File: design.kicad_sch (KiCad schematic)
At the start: 92 parts, among them J1 2601-3108, J10 Conn_01x04, J11 Conn_01x04, J12 Conn_01x03, J13 Conn_01x03, J14 BM04B-SRSS-TB_LF__SN_, J2 2601-3108, J3 2601-3108, J4 TYPE-C-31-M-12, J5 SKEDD-UPDI-4, J6 Conn_01x04, J7 Conn_01x04, J8 Conn_01x04, J9 Conn_01x04, Q1 AO3400A, Q2 AO3400A, SW1 K3-2235S-K1, SW2 K3-2235S-K1, U1 ATtiny1616-S, U2 AP2112K-3.3, U3 CP2105, U4 ATtiny1616-M

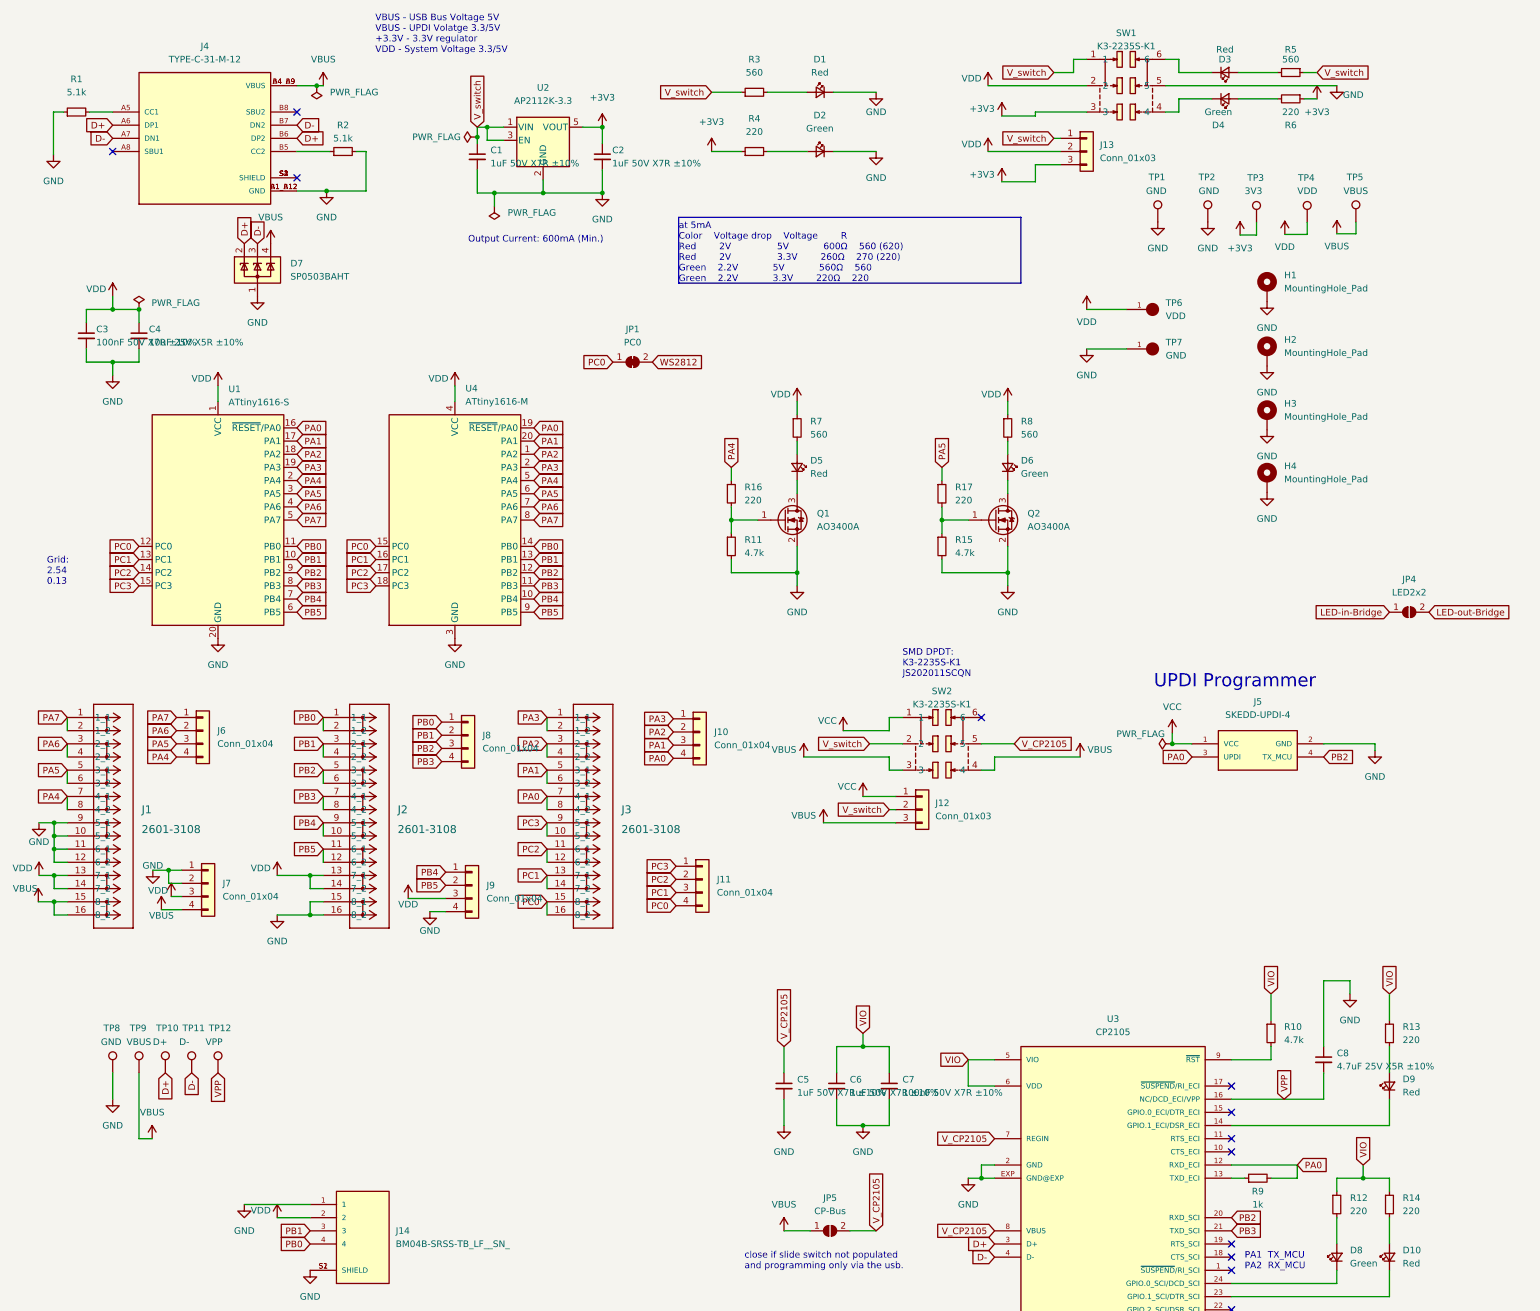
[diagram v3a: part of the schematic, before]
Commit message: add resistor variance
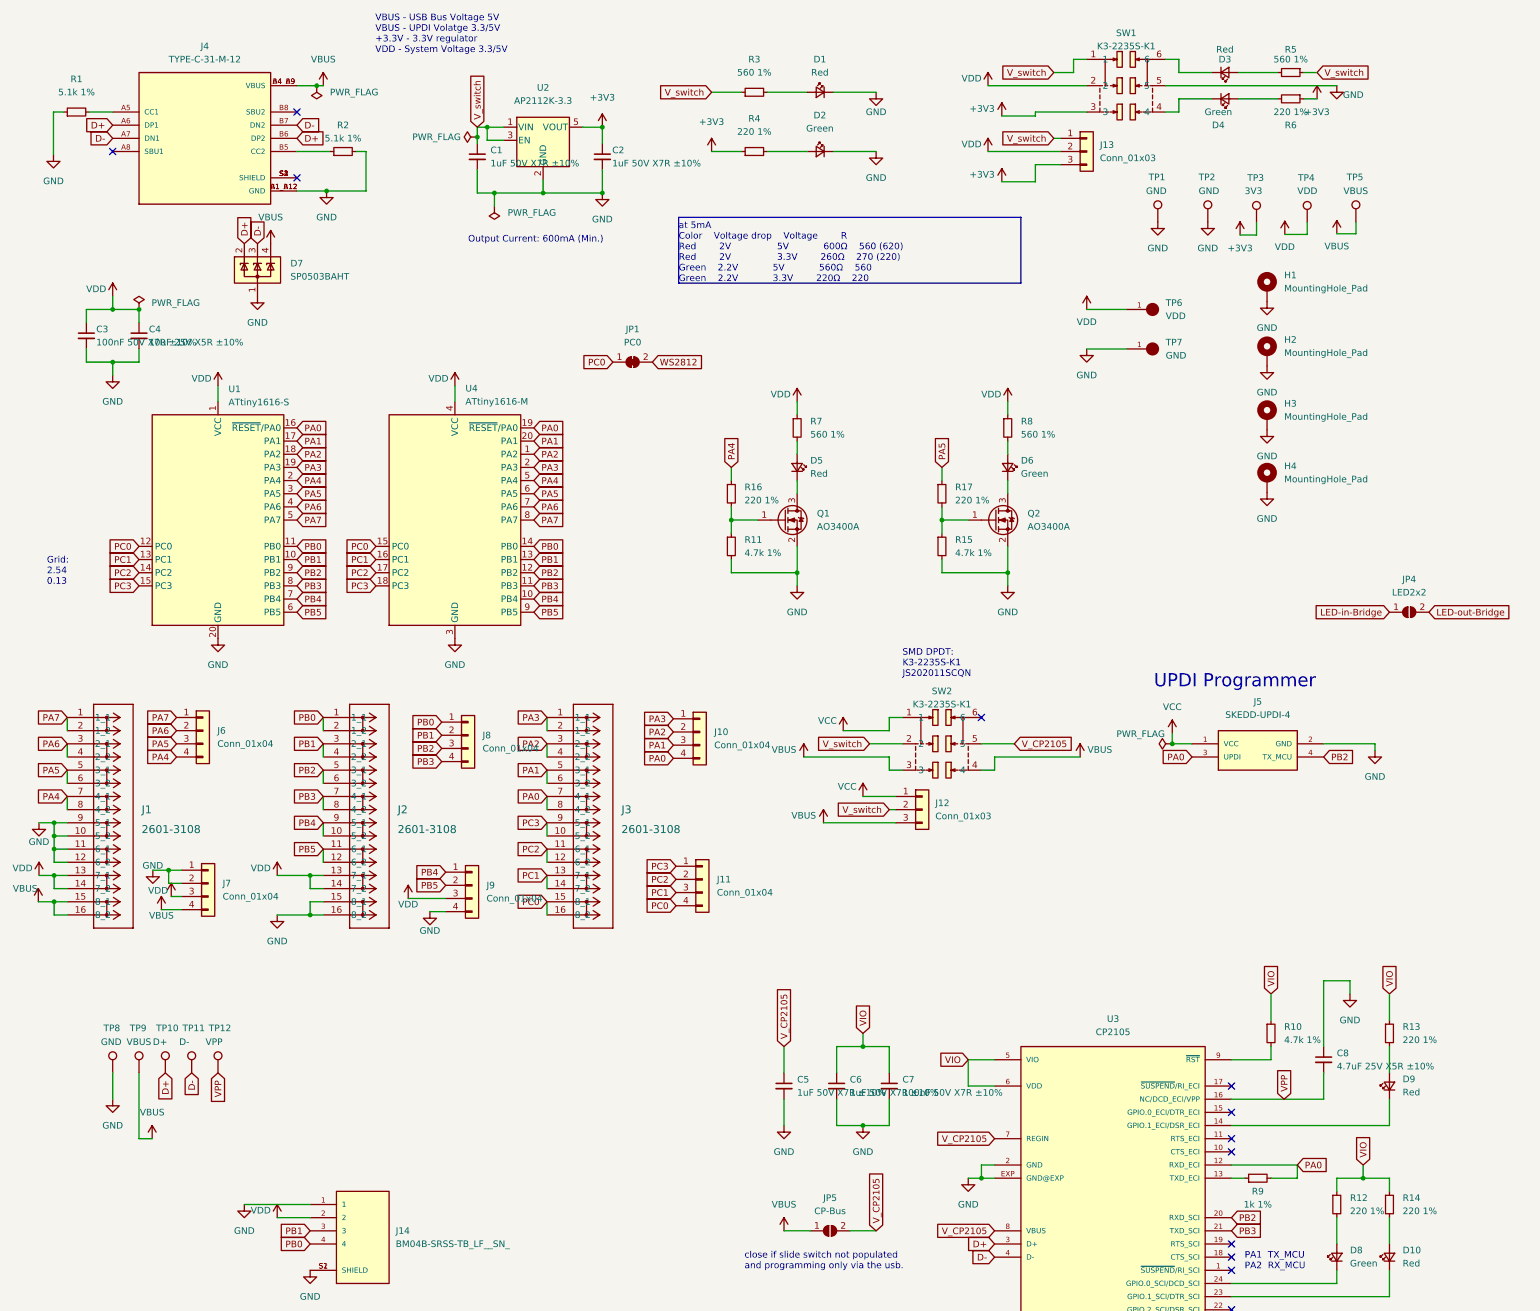
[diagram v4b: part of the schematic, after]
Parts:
- R1, R2: value 5.1k -> 5.1k 1%
- R10, R11, R15: value 4.7k -> 4.7k 1%
- R12, R13, R14, R16, R17, R4, R6: value 220 -> 220 1%
- R3, R5, R7, R8: value 560 -> 560 1%
- R9: value 1k -> 1k 1%
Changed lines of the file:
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@@
       (effects (font (size 1.27 1.27)) (justify left))
     )
-    (property "Value" "220" (id 1) (at 154.94 107.9499 0)
+    (property "Value" "220 1%" (id 1) (at 154.94 107.9499 0)
       (effects (font (size 1.27 1.27)) (justify left))
     )
@@
     (in_bom yes) (on_board yes) (fields_autoplaced)
     (property "Reference" "R4" (id 0) (at 156.845 34.29 90))
-    (property "Value" "220" (id 1) (at 156.845 36.83 90))
+    (property "Value" "220 1%" (id 1) (at 156.845 36.83 90))
     (property "Footprint" "Resistor_SMD:R_0805_2012Metric" (id 2) (at 156.845 40.64 0)
       (effects (font (size 1.27 1.27)) hide)
@@
       (effects (font (size 1.27 1.27)) (justify left))
     )
-    (property "Value" "220" (id 1) (at 195.58 107.9499 0)
+    (property "Value" "220 1%" (id 1) (at 195.58 107.9499 0)
       (effects (font (size 1.27 1.27)) (justify left))
     )
@@
     (in_bom yes) (on_board yes)
     (property "Reference" "R1" (id 0) (at 26.035 26.67 90))
-    (property "Value" "5.1k" (id 1) (at 26.035 29.21 90))
+    (property "Value" "5.1k 1%" (id 1) (at 26.035 29.21 90))
     (property "Footprint" "Resistor_SMD:R_0805_2012Metric" (id 2) (at 26.035 33.02 0)
       (effects (font (size 1.27 1.27)) hide)
@@
       (effects (font (size 1.27 1.27)) (justify left))
     )
-    (property "Value" "560" (id 1) (at 167.64 95.2499 0)
+    (property "Value" "560 1%" (id 1) (at 167.64 95.2499 0)
       (effects (font (size 1.27 1.27)) (justify left))
     )
@@
       (effects (font (size 1.27 1.27)) (justify left))
     )
-    (property "Value" "560" (id 1) (at 208.28 95.2499 0)
+    (property "Value" "560 1%" (id 1) (at 208.28 95.2499 0)
       (effects (font (size 1.27 1.27)) (justify left))
     )
@@
     (in_bom yes) (on_board yes) (fields_autoplaced)
     (property "Reference" "R3" (id 0) (at 156.845 22.86 90))
-    (property "Value" "560" (id 1) (at 156.845 25.4 90))
+    (property "Value" "560 1%" (id 1) (at 156.845 25.4 90))
     (property "Footprint" "Resistor_SMD:R_0805_2012Metric" (id 2) (at 156.845 29.21 0)
       (effects (font (size 1.27 1.27)) hide)
@@
       (effects (font (size 1.27 1.27)) (justify left))
     )
-    (property "Value" "220" (id 1) (at 281.94 245.1099 0)
+    (property "Value" "220 1%" (id 1) (at 281.94 245.1099 0)
       (effects (font (size 1.27 1.27)) (justify left))
     )
@@
     (in_bom yes) (on_board yes)
     (property "Reference" "R9" (id 0) (at 254 241.3 90))
-    (property "Value" "1k" (id 1) (at 254 243.84 90))
+    (property "Value" "1k 1%" (id 1) (at 254 243.84 90))
     (property "Footprint" "Resistor_SMD:R_0805_2012Metric" (id 2) (at 254 238.76 0)
       (effects (font (size 1.27 1.27)) hide)
@@
     (in_bom yes) (on_board yes)
     (property "Reference" "R6" (id 0) (at 260.35 35.56 90))
-    (property "Value" "220" (id 1) (at 260.35 33.02 90))
+    (property "Value" "220 1%" (id 1) (at 260.35 33.02 90))
     (property "Footprint" "Resistor_SMD:R_0805_2012Metric" (id 2) (at 260.35 30.48 0)
       (effects (font (size 1.27 1.27)) hide)
@@
       (effects (font (size 1.27 1.27)) (justify left))
     )
-    (property "Value" "4.7k" (id 1) (at 259.08 212.0899 0)
+    (property "Value" "4.7k 1%" (id 1) (at 259.08 212.0899 0)
       (effects (font (size 1.27 1.27)) (justify left))
     )
@@
       (effects (font (size 1.27 1.27)) (justify left))
     )
-    (property "Value" "220" (id 1) (at 281.94 212.0899 0)
+    (property "Value" "220 1%" (id 1) (at 281.94 212.0899 0)
       (effects (font (size 1.27 1.27)) (justify left))
     )
@@
     (in_bom yes) (on_board yes)
     (property "Reference" "R5" (id 0) (at 260.35 20.955 90))
-    (property "Value" "560" (id 1) (at 260.35 22.86 90))
+    (property "Value" "560 1%" (id 1) (at 260.35 22.86 90))
     (property "Footprint" "Resistor_SMD:R_0805_2012Metric" (id 2) (at 260.35 25.4 0)
       (effects (font (size 1.27 1.27)) hide)
@@
     (in_bom yes) (on_board yes)
     (property "Reference" "R2" (id 0) (at 77.47 35.56 90))
-    (property "Value" "5.1k" (id 1) (at 77.47 38.1 90))
+    (property "Value" "5.1k 1%" (id 1) (at 77.47 38.1 90))
     (property "Footprint" "Resistor_SMD:R_0805_2012Metric" (id 2) (at 77.47 40.64 0)
       (effects (font (size 1.27 1.27)) hide)
@@
       (effects (font (size 1.27 1.27)) (justify left))
     )
-    (property "Value" "220" (id 1) (at 271.78 245.1099 0)
+    (property "Value" "220 1%" (id 1) (at 271.78 245.1099 0)
       (effects (font (size 1.27 1.27)) (justify left))
     )
@@
       (effects (font (size 1.27 1.27)) (justify left))
     )
-    (property "Value" "4.7k" (id 1) (at 154.94 118.1099 0)
+    (property "Value" "4.7k 1%" (id 1) (at 154.94 118.1099 0)
       (effects (font (size 1.27 1.27)) (justify left))
     )
@@
       (effects (font (size 1.27 1.27)) (justify left))
     )
-    (property "Value" "4.7k" (id 1) (at 195.58 118.1099 0)
+    (property "Value" "4.7k 1%" (id 1) (at 195.58 118.1099 0)
       (effects (font (size 1.27 1.27)) (justify left))
     )
@@
     )
     (path "/2d960c53-92c0-4508-8c86-63a3901a9176"
-      (reference "R1") (unit 1) (value "5.1k") (footprint "Resistor_SMD:R_0805_2012Metric")
+      (reference "R1") (unit 1) (value "5.1k 1%") (footprint "Resistor_SMD:R_0805_2012Metric")
     )
     (path "/c779e7c4-17e4-477d-a6d1-52b907c8df98"
-      (reference "R2") (unit 1) (value "5.1k") (footprint "Resistor_SMD:R_0805_2012Metric")
+      (reference "R2") (unit 1) (value "5.1k 1%") (footprint "Resistor_SMD:R_0805_2012Metric")
     )
     (path "/484da902-60c6-4980-9a91-4f667955b0e8"
-      (reference "R3") (unit 1) (value "560") (footprint "Resistor_SMD:R_0805_2012Metric")
+      (reference "R3") (unit 1) (value "560 1%") (footprint "Resistor_SMD:R_0805_2012Metric")
     )
     (path "/0e89c407-3205-4c62-a491-3291420c5ad0"
-      (reference "R4") (unit 1) (value "220") (footprint "Resistor_SMD:R_0805_2012Metric")
+      (reference "R4") (unit 1) (value "220 1%") (footprint "Resistor_SMD:R_0805_2012Metric")
     )
     (path "/bcf61e20-6cf8-46b9-9f95-d5e631d20676"
-      (reference "R5") (unit 1) (value "560") (footprint "Resistor_SMD:R_0805_2012Metric")
+      (reference "R5") (unit 1) (value "560 1%") (footprint "Resistor_SMD:R_0805_2012Metric")
     )
     (path "/72f13b47-0aa0-4ea7-a1ab-fd196a1c1813"
-      (reference "R6") (unit 1) (value "220") (footprint "Resistor_SMD:R_0805_2012Metric")
+      (reference "R6") (unit 1) (value "220 1%") (footprint "Resistor_SMD:R_0805_2012Metric")
     )
     (path "/42965c34-d4b3-417b-ac70-1b8024990edc"
-      (reference "R7") (unit 1) (value "560") (footprint "Resistor_SMD:R_0805_2012Metric")
+      (reference "R7") (unit 1) (value "560 1%") (footprint "Resistor_SMD:R_0805_2012Metric")
     )
     (path "/44e2dfc4-2c8c-4871-9b80-83ccfe223af7"
-      (reference "R8") (unit 1) (value "560") (footprint "Resistor_SMD:R_0805_2012Metric")
+      (reference "R8") (unit 1) (value "560 1%") (footprint "Resistor_SMD:R_0805_2012Metric")
     )
     (path "/5d57726e-0434-4089-b57f-b38108417a5f"
-      (reference "R9") (unit 1) (value "1k") (footprint "Resistor_SMD:R_0805_2012Metric")
+      (reference "R9") (unit 1) (value "1k 1%") (footprint "Resistor_SMD:R_0805_2012Metric")
     )
     (path "/97ff0e12-c8c6-4e4c-ac54-7a23a9d49f5e"
-      (reference "R10") (unit 1) (value "4.7k") (footprint "Resistor_SMD:R_0805_2012Metric")
+      (reference "R10") (unit 1) (value "4.7k 1%") (footprint "Resistor_SMD:R_0805_2012Metric")
     )
     (path "/eae5ea89-345f-400b-bbc1-315b0f92403d"
-      (reference "R11") (unit 1) (value "4.7k") (footprint "Resistor_SMD:R_0805_2012Metric")
+      (reference "R11") (unit 1) (value "4.7k 1%") (footprint "Resistor_SMD:R_0805_2012Metric")
     )
     (path "/d3f3b6a4-65f9-4d68-88bb-38ec87453a14"
-      (reference "R12") (unit 1) (value "220") (footprint "Resistor_SMD:R_0805_2012Metric")
+      (reference "R12") (unit 1) (value "220 1%") (footprint "Resistor_SMD:R_0805_2012Metric")
     )
     (path "/a758422c-1795-447b-8ef1-8283da654354"
-      (reference "R13") (unit 1) (value "220") (footprint "Resistor_SMD:R_0805_2012Metric")
+      (reference "R13") (unit 1) (value "220 1%") (footprint "Resistor_SMD:R_0805_2012Metric")
     )
     (path "/5799ac00-06e7-4fa3-91a4-ef96b7ec0384"
-      (reference "R14") (unit 1) (value "220") (footprint "Resistor_SMD:R_0805_2012Metric")
+      (reference "R14") (unit 1) (value "220 1%") (footprint "Resistor_SMD:R_0805_2012Metric")
     )
     (path "/fa4d6553-7f09-4a6e-9c40-3ec022302ac5"
-      (reference "R15") (unit 1) (value "4.7k") (footprint "Resistor_SMD:R_0805_2012Metric")
+      (reference "R15") (unit 1) (value "4.7k 1%") (footprint "Resistor_SMD:R_0805_2012Metric")
     )
     (path "/054880c8-c6d2-48c6-bac5-eb0eb8670720"
-      (reference "R16") (unit 1) (value "220") (footprint "Resistor_SMD:R_0805_2012Metric")
+      (reference "R16") (unit 1) (value "220 1%") (footprint "Resistor_SMD:R_0805_2012Metric")
     )
     (path "/184973bb-9061-457b-885d-f342e181cc30"
-      (reference "R17") (unit 1) (value "220") (footprint "Resistor_SMD:R_0805_2012Metric")
+      (reference "R17") (unit 1) (value "220 1%") (footprint "Resistor_SMD:R_0805_2012Metric")
     )
     (path "/3c015059-970d-4b9b-a360-1a6bff162160"

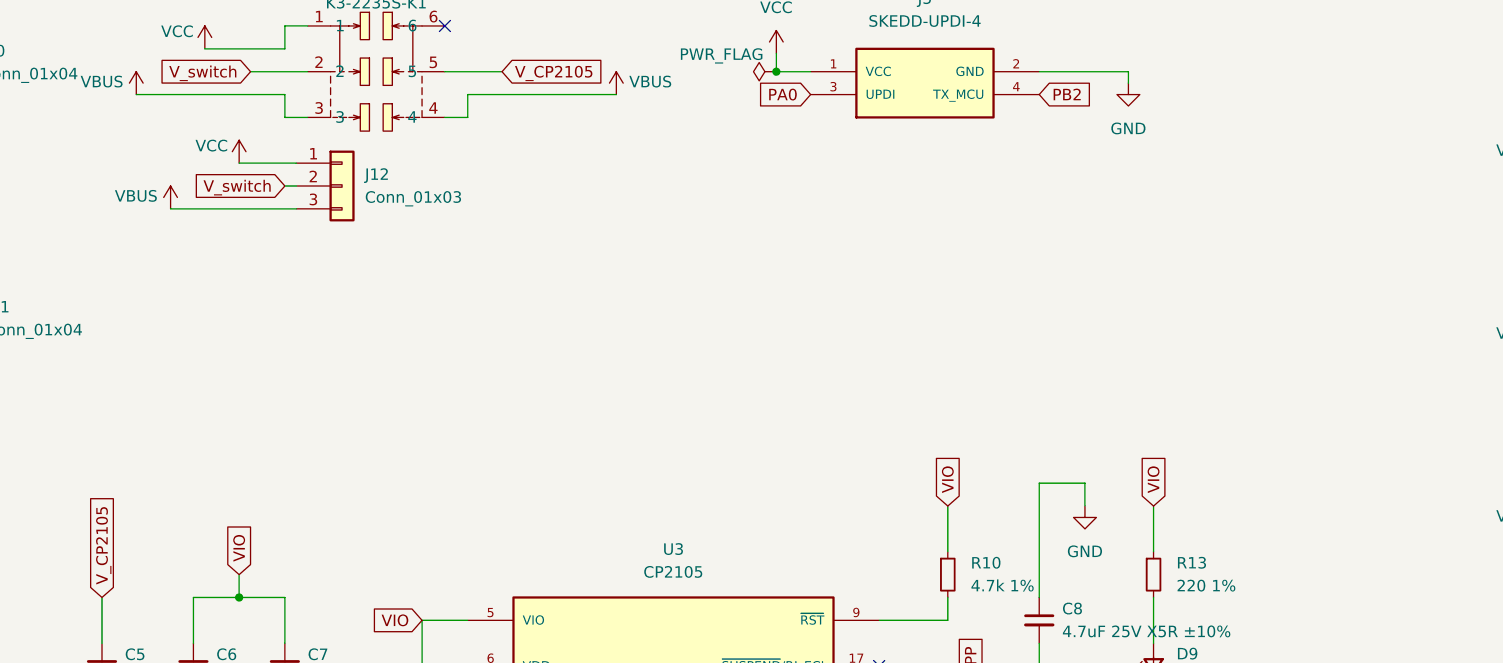
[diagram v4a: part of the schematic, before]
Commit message: add LM66200DRLR
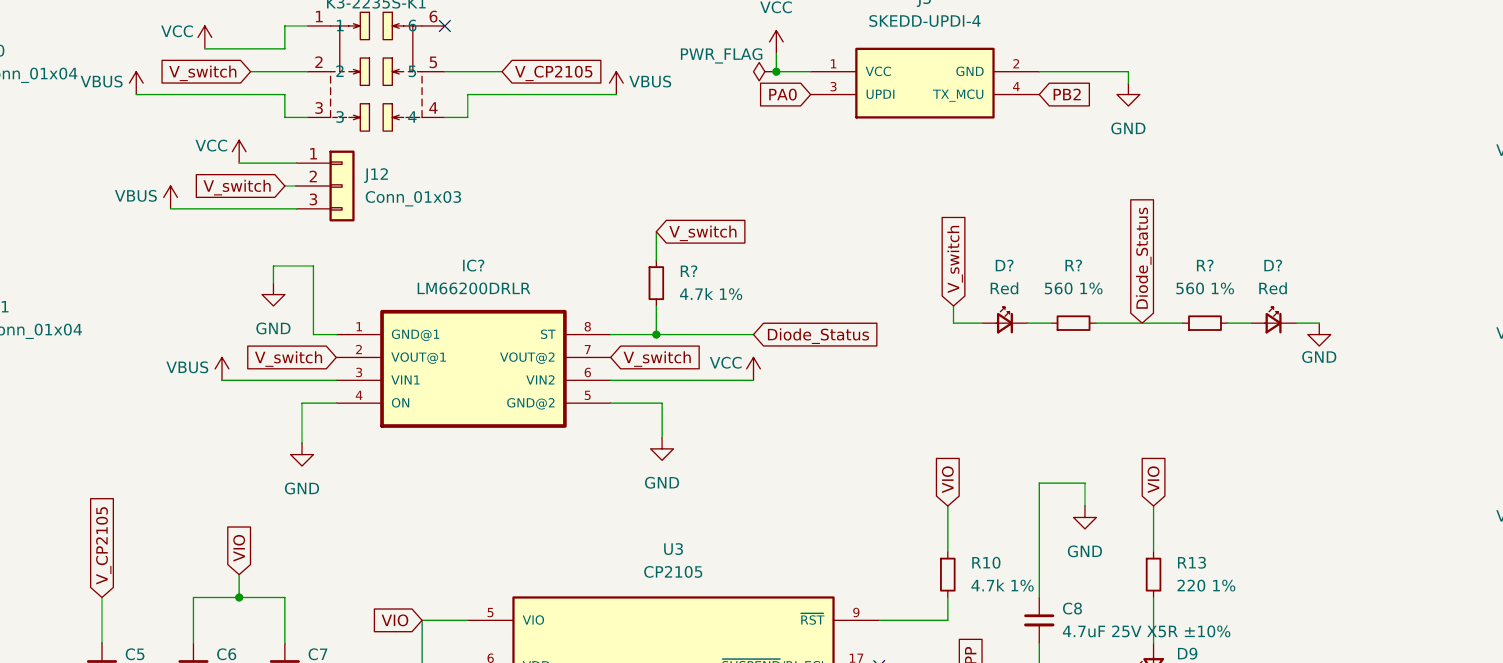
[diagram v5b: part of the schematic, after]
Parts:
- added D? (x2): Red, LED_SMD:LED_0805_2012Metric, symbol Device:LED_Small
- added IC?: LM66200DRLR, Snapeda:LM66200DRLR_SOT8, symbol Snapeda:LM66200DRLR
- added R?: 4.7k 1%, Resistor_SMD:R_0805_2012Metric, symbol Device:R_Small
- added R? (x2): 560 1%, Resistor_SMD:R_0805_2012Metric, symbol Device:R_Small
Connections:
- net GND: now also D?.1 (K), IC?.1 (GND@1), IC?.4 (ON), IC?.5 (GND@2)
- net VBUS: now also IC?.3 (VIN1)
- net VCC: now also IC?.6 (VIN2)
- net V_switch: now also D?.2 (A), IC?.2 (VOUT@1), IC?.7 (VOUT@2), R?.1
- new net: D?.1 (K), R?.1
- new net: D?.2 (A), R?.2
- new net Diode_Status: IC?.8 (ST), R?.1, R?.2, R?.2
